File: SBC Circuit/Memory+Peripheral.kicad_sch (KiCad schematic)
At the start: 19 parts, among them J5 Conn_01x03_Pin, J6 Conn_01x08_Pin, J7 Conn_01x06_Pin, U3 68681, U4 MCM6206CP, U5 MCM6206CP, U6 28C256, U7 28C256, X2 EC11

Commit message: Assign Footprints
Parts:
- C16, C17, C18, C19, C20, C21, C22, C23, C24, C25: footprint (none) -> Capacitor_THT:CP_Box_L5.50mm_W4.00mm_P2.50mm_NonPolarized
- J5: footprint (none) -> Connector_PinHeader_2.54mm:PinHeader_1x03_P2.54mm_Vertical
- J6: footprint (none) -> Connector_PinHeader_2.54mm:PinHeader_1x08_P2.54mm_Vertical
- J7: footprint (none) -> Connector_PinHeader_2.54mm:PinHeader_1x06_P2.54mm_Vertical
- U3: footprint (none) -> Package_DIP:DIP-40_W15.24mm_Socket
- U4, U5: footprint Package_DIP:DIP-28_W15.24mm -> Package_DIP:DIP-28_W7.62mm_Socket
- U6, U7: footprint (none) -> Package_DIP:DIP-28_W15.24mm_Socket
- X2: footprint Oscillator:Oscillator_SeikoEpson_SG-8002DC -> Oscillator:Oscillator_DIP-8
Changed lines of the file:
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@@
       (effects (font (size 1.27 1.27)))
     )
-    (property "Footprint" "" (at 68.58 115.2652 0)
+    (property "Footprint" "Capacitor_THT:CP_Box_L5.50mm_W4.00mm_P2.50mm_NonPolarized" (at 68.58 115.2652 0)
       (effects (font (size 1.27 1.27)) hide)
     )
@@
       (effects (font (size 1.27 1.27)))
     )
-    (property "Footprint" "" (at 68.58 108.2548 0)
+    (property "Footprint" "Capacitor_THT:CP_Box_L5.50mm_W4.00mm_P2.50mm_NonPolarized" (at 68.58 108.2548 0)
       (effects (font (size 1.27 1.27)) hide)
     )
@@
       (effects (font (size 1.27 1.27)) hide)
     )
-    (property "Footprint" "Package_DIP:DIP-28_W15.24mm" (at 130.81 67.31 0)
+    (property "Footprint" "Package_DIP:DIP-28_W7.62mm_Socket" (at 130.81 67.31 0)
       (effects (font (size 1.27 1.27)) hide)
     )
@@
       (effects (font (size 1.27 1.27)))
     )
-    (property "Footprint" "" (at 242.57 49.8348 0)
+    (property "Footprint" "Capacitor_THT:CP_Box_L5.50mm_W4.00mm_P2.50mm_NonPolarized" (at 242.57 49.8348 0)
       (effects (font (size 1.27 1.27)) hide)
     )
@@
       (effects (font (size 1.27 1.27)) hide)
     )
-    (property "Footprint" "Package_DIP:DIP-28_W15.24mm" (at 54.61 67.31 0)
+    (property "Footprint" "Package_DIP:DIP-28_W7.62mm_Socket" (at 54.61 67.31 0)
       (effects (font (size 1.27 1.27)) hide)
     )
@@
       (effects (font (size 1.27 1.27)))
     )
-    (property "Footprint" "" (at 242.57 56.8452 0)
+    (property "Footprint" "Capacitor_THT:CP_Box_L5.50mm_W4.00mm_P2.50mm_NonPolarized" (at 242.57 56.8452 0)
       (effects (font (size 1.27 1.27)) hide)
     )
@@
       (effects (font (size 1.27 1.27)) (justify left))
     )
-    (property "Footprint" "Oscillator:Oscillator_SeikoEpson_SG-8002DC" (at 201.93 60.96 0)
+    (property "Footprint" "Oscillator:Oscillator_DIP-8" (at 201.93 60.96 0)
       (effects (font (size 1.27 1.27)) hide)
     )
@@
       (effects (font (size 1.27 1.27)))
     )
-    (property "Footprint" "" (at 66.04 36.5252 0)
+    (property "Footprint" "Capacitor_THT:CP_Box_L5.50mm_W4.00mm_P2.50mm_NonPolarized" (at 66.04 36.5252 0)
       (effects (font (size 1.27 1.27)) hide)
     )
@@
       (effects (font (size 1.27 1.27)))
     )
-    (property "Footprint" "" (at 144.78 115.2652 0)
+    (property "Footprint" "Capacitor_THT:CP_Box_L5.50mm_W4.00mm_P2.50mm_NonPolarized" (at 144.78 115.2652 0)
       (effects (font (size 1.27 1.27)) hide)
     )
@@
       (effects (font (size 1.27 1.27)))
     )
-    (property "Footprint" "" (at 144.78 108.2548 0)
+    (property "Footprint" "Capacitor_THT:CP_Box_L5.50mm_W4.00mm_P2.50mm_NonPolarized" (at 144.78 108.2548 0)
       (effects (font (size 1.27 1.27)) hide)
     )
@@
       (effects (font (size 1.27 1.27)))
     )
-    (property "Footprint" "" (at 142.24 36.5252 0)
+    (property "Footprint" "Capacitor_THT:CP_Box_L5.50mm_W4.00mm_P2.50mm_NonPolarized" (at 142.24 36.5252 0)
       (effects (font (size 1.27 1.27)) hide)
     )
@@
       (effects (font (size 1.27 1.27)))
     )
-    (property "Footprint" "" (at 66.04 29.5148 0)
+    (property "Footprint" "Capacitor_THT:CP_Box_L5.50mm_W4.00mm_P2.50mm_NonPolarized" (at 66.04 29.5148 0)
       (effects (font (size 1.27 1.27)) hide)
     )
@@
       (effects (font (size 1.27 1.27)) (justify right))
     )
-    (property "Footprint" "" (at 259.08 35.56 0)
+    (property "Footprint" "Connector_PinHeader_2.54mm:PinHeader_1x03_P2.54mm_Vertical" (at 259.08 35.56 0)
       (effects (font (size 1.27 1.27)) hide)
     )
@@
       (effects (font (size 1.27 1.27)) (justify right))
     )
-    (property "Footprint" "" (at 265.43 110.49 0)
+    (property "Footprint" "Connector_PinHeader_2.54mm:PinHeader_1x06_P2.54mm_Vertical" (at 265.43 110.49 0)
       (effects (font (size 1.27 1.27)) hide)
     )
@@
       (effects (font (size 1.27 1.27)))
     )
-    (property "Footprint" "" (at 231.14 97.79 0)
+    (property "Footprint" "Package_DIP:DIP-40_W15.24mm_Socket" (at 231.14 97.79 0)
       (effects (font (size 1.27 1.27)) hide)
     )
@@
       (effects (font (size 1.27 1.27)))
     )
-    (property "Footprint" "" (at 142.24 29.5148 0)
+    (property "Footprint" "Capacitor_THT:CP_Box_L5.50mm_W4.00mm_P2.50mm_NonPolarized" (at 142.24 29.5148 0)
       (effects (font (size 1.27 1.27)) hide)
     )
@@
       (effects (font (size 1.27 1.27)) (justify right))
     )
-    (property "Footprint" "" (at 265.43 90.17 0)
+    (property "Footprint" "Connector_PinHeader_2.54mm:PinHeader_1x08_P2.54mm_Vertical" (at 265.43 90.17 0)
       (effects (font (size 1.27 1.27)) hide)
     )
@@
       (effects (font (size 1.27 1.27)) hide)
     )
-    (property "Footprint" "" (at 57.15 148.59 0)
+    (property "Footprint" "Package_DIP:DIP-28_W15.24mm_Socket" (at 57.15 148.59 0)
       (effects (font (size 1.27 1.27)) hide)
     )
@@
       (effects (font (size 1.27 1.27)) hide)
     )
-    (property "Footprint" "" (at 133.35 148.59 0)
-      (effects (font (size 1.27 1.27)) hide)
-    )
+    (property "Footprint" "Package_DIP:DIP-28_W15.24mm_Socket" (at 133.35 148.59 0)
+      (effects (font (size 1.27 1.27)) hide)
+    )

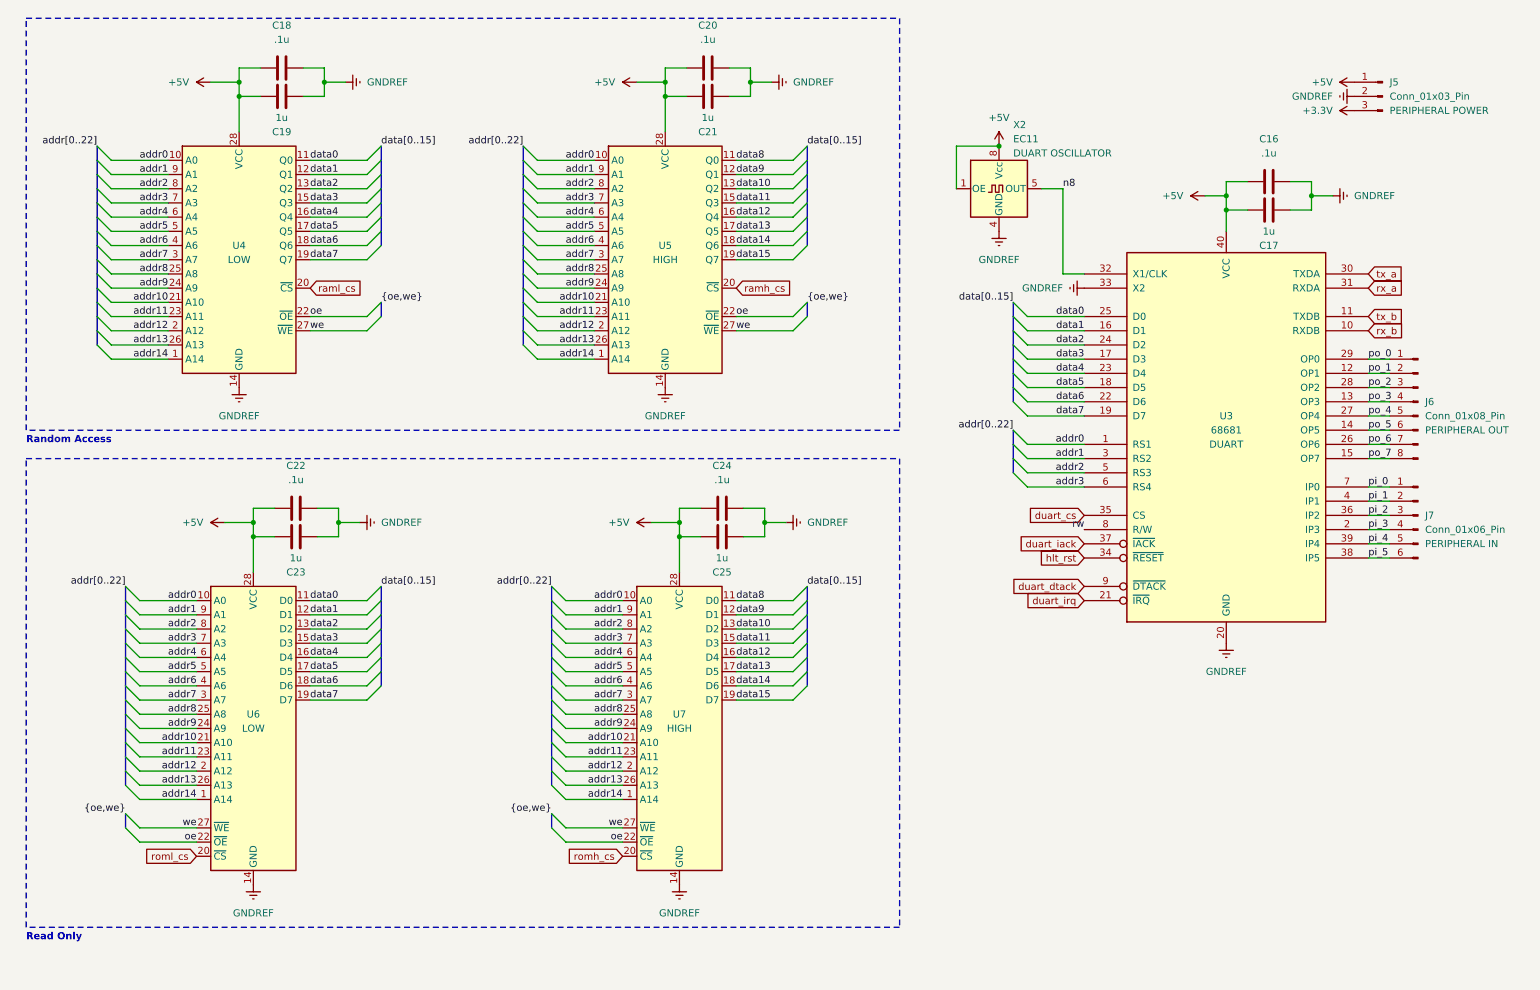
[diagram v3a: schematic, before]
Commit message: Fix intersheet bus issues
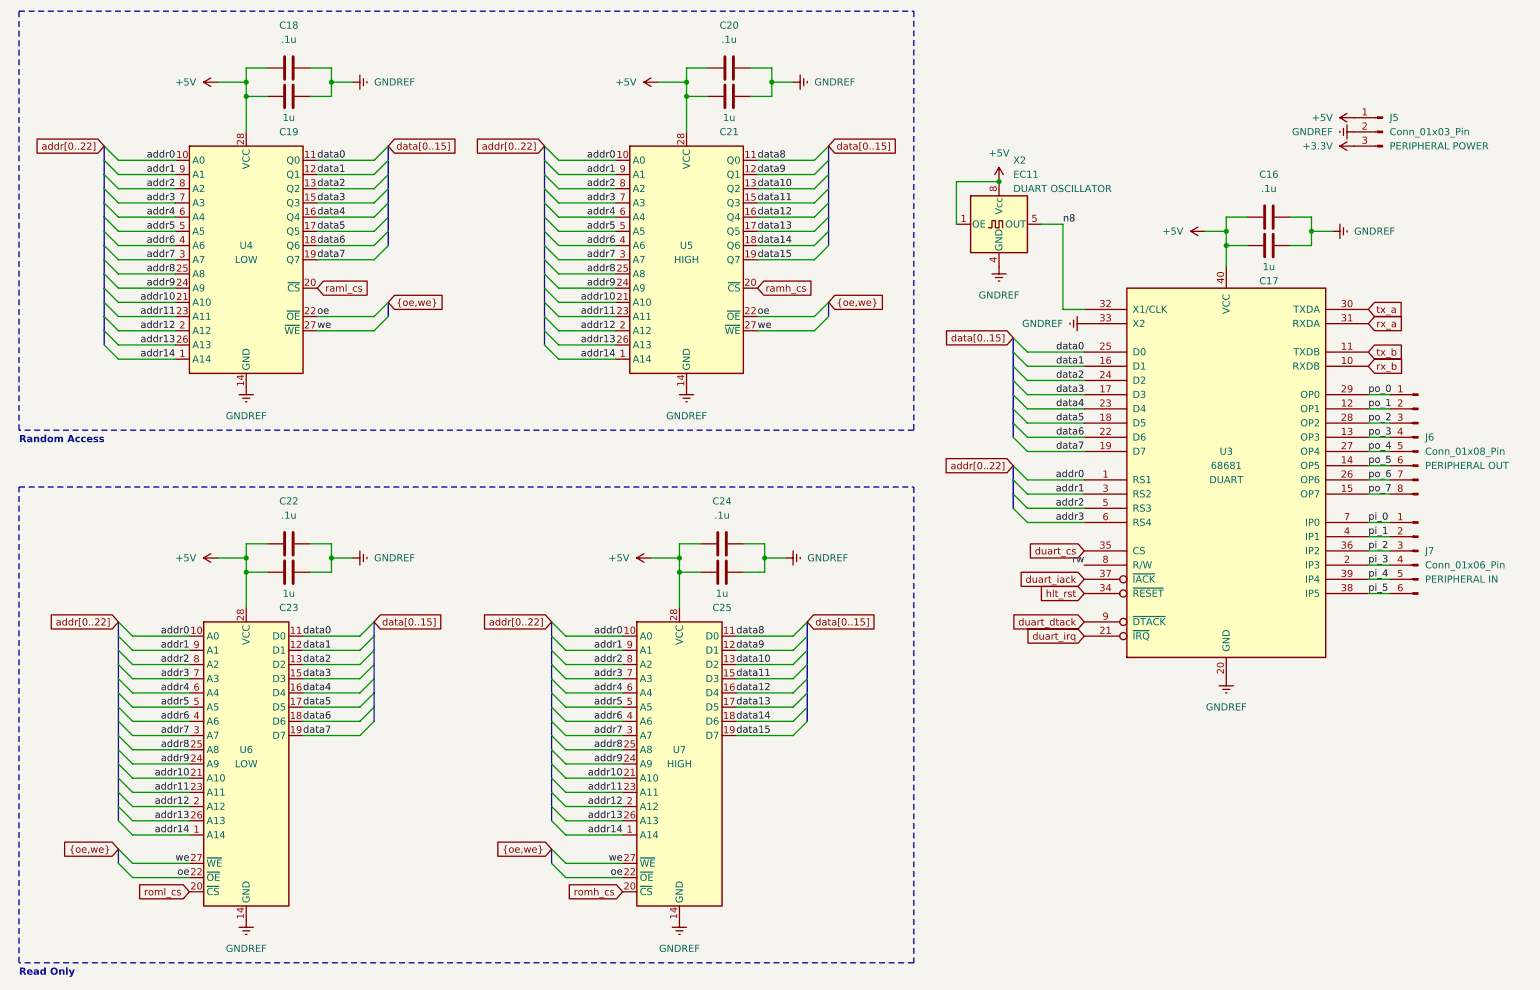
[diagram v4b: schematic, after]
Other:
- moved on the sheet: C16, C17, C18, C19, C20, C21, C22, C23, C24, C25, J5, J6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

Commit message: PCB CPLD to MPU lines wired
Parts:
- C16, C17, C18, C19, C20, C21, C22, C23, C24, C25: footprint Capacitor_THT:CP_Box_L5.50mm_W4.00mm_P2.50mm_NonPolarized -> Capacitor_THT:CP_Disc_L5.50mm_W4.00mm_P2.50mm_NonPolarized
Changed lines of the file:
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@@
   (title_block
     (title "MEMORY & PERIPHERAL")
-    (date "2024-01-22")
-    (rev "0.3")
+    (date "2024-01-24")
+    (rev "0.4")
     (company "LeTourneau University")
     (comment 1 "Richard Homan")
@@
       (effects (font (size 1.27 1.27)))
     )
-    (property "Footprint" "Capacitor_THT:CP_Box_L5.50mm_W4.00mm_P2.50mm_NonPolarized" (at 67.31 121.6152 0)
+    (property "Footprint" "Capacitor_THT:CP_Disc_L5.50mm_W4.00mm_P2.50mm_NonPolarized" (at 67.31 121.6152 0)
       (effects (font (size 1.27 1.27)) hide)
     )
@@
       (effects (font (size 1.27 1.27)))
     )
-    (property "Footprint" "Capacitor_THT:CP_Box_L5.50mm_W4.00mm_P2.50mm_NonPolarized" (at 67.31 114.6048 0)
+    (property "Footprint" "Capacitor_THT:CP_Disc_L5.50mm_W4.00mm_P2.50mm_NonPolarized" (at 67.31 114.6048 0)
       (effects (font (size 1.27 1.27)) hide)
     )
@@
       (effects (font (size 1.27 1.27)))
     )
-    (property "Footprint" "Capacitor_THT:CP_Box_L5.50mm_W4.00mm_P2.50mm_NonPolarized" (at 242.57 56.1848 0)
+    (property "Footprint" "Capacitor_THT:CP_Disc_L5.50mm_W4.00mm_P2.50mm_NonPolarized" (at 242.57 56.1848 0)
       (effects (font (size 1.27 1.27)) hide)
     )
@@
       (effects (font (size 1.27 1.27)))
     )
-    (property "Footprint" "Capacitor_THT:CP_Box_L5.50mm_W4.00mm_P2.50mm_NonPolarized" (at 242.57 63.1952 0)
+    (property "Footprint" "Capacitor_THT:CP_Disc_L5.50mm_W4.00mm_P2.50mm_NonPolarized" (at 242.57 63.1952 0)
       (effects (font (size 1.27 1.27)) hide)
     )
@@
       (effects (font (size 1.27 1.27)))
     )
-    (property "Footprint" "Capacitor_THT:CP_Box_L5.50mm_W4.00mm_P2.50mm_NonPolarized" (at 67.31 36.5252 0)
+    (property "Footprint" "Capacitor_THT:CP_Disc_L5.50mm_W4.00mm_P2.50mm_NonPolarized" (at 67.31 36.5252 0)
       (effects (font (size 1.27 1.27)) hide)
     )
@@
       (effects (font (size 1.27 1.27)))
     )
-    (property "Footprint" "Capacitor_THT:CP_Box_L5.50mm_W4.00mm_P2.50mm_NonPolarized" (at 144.78 121.6152 0)
+    (property "Footprint" "Capacitor_THT:CP_Disc_L5.50mm_W4.00mm_P2.50mm_NonPolarized" (at 144.78 121.6152 0)
       (effects (font (size 1.27 1.27)) hide)
     )
@@
       (effects (font (size 1.27 1.27)))
     )
-    (property "Footprint" "Capacitor_THT:CP_Box_L5.50mm_W4.00mm_P2.50mm_NonPolarized" (at 144.78 114.6048 0)
+    (property "Footprint" "Capacitor_THT:CP_Disc_L5.50mm_W4.00mm_P2.50mm_NonPolarized" (at 144.78 114.6048 0)
       (effects (font (size 1.27 1.27)) hide)
     )
@@
       (effects (font (size 1.27 1.27)))
     )
-    (property "Footprint" "Capacitor_THT:CP_Box_L5.50mm_W4.00mm_P2.50mm_NonPolarized" (at 146.05 36.5252 0)
+    (property "Footprint" "Capacitor_THT:CP_Disc_L5.50mm_W4.00mm_P2.50mm_NonPolarized" (at 146.05 36.5252 0)
       (effects (font (size 1.27 1.27)) hide)
     )
@@
       (effects (font (size 1.27 1.27)))
     )
-    (property "Footprint" "Capacitor_THT:CP_Box_L5.50mm_W4.00mm_P2.50mm_NonPolarized" (at 67.31 29.5148 0)
+    (property "Footprint" "Capacitor_THT:CP_Disc_L5.50mm_W4.00mm_P2.50mm_NonPolarized" (at 67.31 29.5148 0)
       (effects (font (size 1.27 1.27)) hide)
     )
@@
       (effects (font (size 1.27 1.27)))
     )
-    (property "Footprint" "Capacitor_THT:CP_Box_L5.50mm_W4.00mm_P2.50mm_NonPolarized" (at 146.05 29.5148 0)
-      (effects (font (size 1.27 1.27)) hide)
-    )
+    (property "Footprint" "Capacitor_THT:CP_Disc_L5.50mm_W4.00mm_P2.50mm_NonPolarized" (at 146.05 29.5148 0)
+      (effects (font (size 1.27 1.27)) hide)
+    )

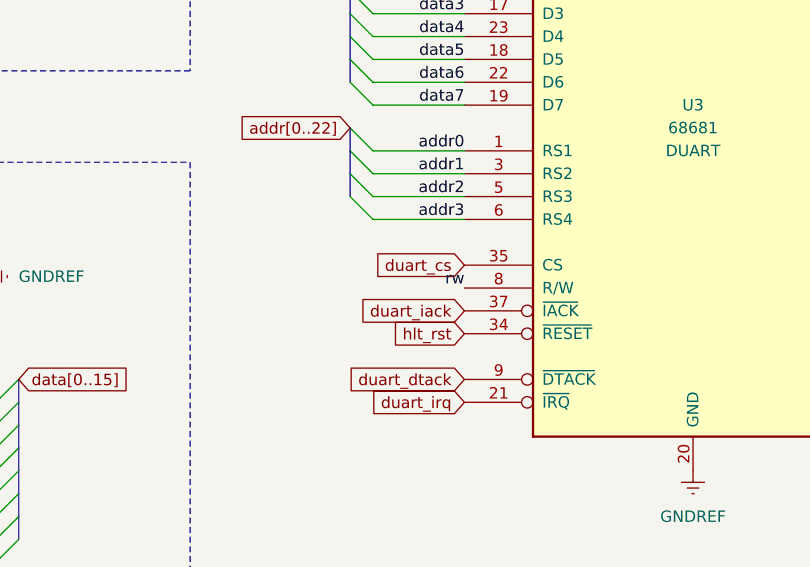
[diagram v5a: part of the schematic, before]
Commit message: Finish DUART lines
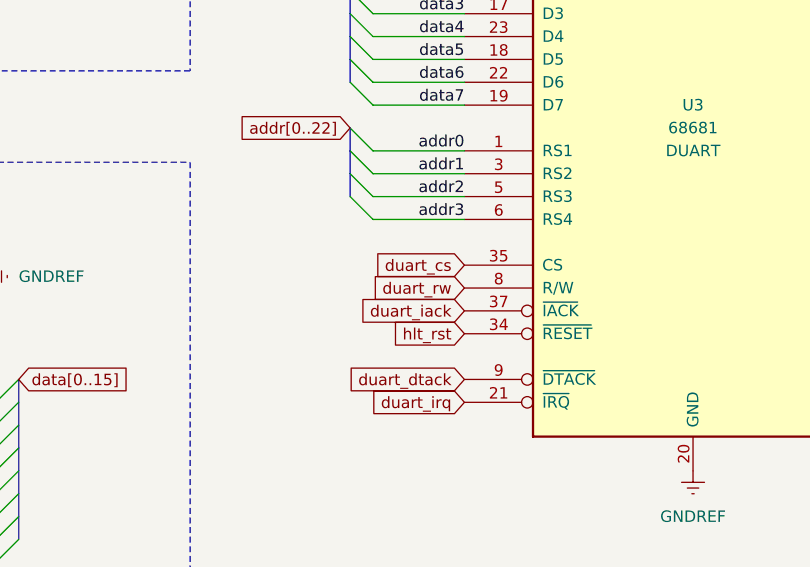
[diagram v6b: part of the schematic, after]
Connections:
- net rw renamed duart_rw
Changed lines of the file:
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@@
     )
-  )
-  (label "rw" (at 205.74 119.38 180) (fields_autoplaced)
-    (effects (font (size 1.27 1.27)) (justify right bottom))
   )
   (label "n8" (at 201.93 58.42 0) (fields_autoplaced)
@@
       (effects (font (size 1.27 1.27)) (justify right) hide)
     )
+  )
+  (global_label "duart_rw" (shape input) (at 205.74 119.38 180) (fields_autoplaced)
+    (effects (font (size 1.27 1.27)) (justify right))
+    (property "Intersheetrefs" "${INTERSHEET_REFS}" (at 194.7116 119.38 0)
+      (effects (font (size 1.27 1.27)) (justify right) hide)
+    )
+    (property "Netclass" "signal" (at 205.74 121.5708 0)
+      (effects (font (size 1.27 1.27)) (justify right) hide)
+    )
